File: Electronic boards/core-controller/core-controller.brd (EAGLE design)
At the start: 100 x 80 mm, 15 parts, among them IC1 ATMEGA88-THIN

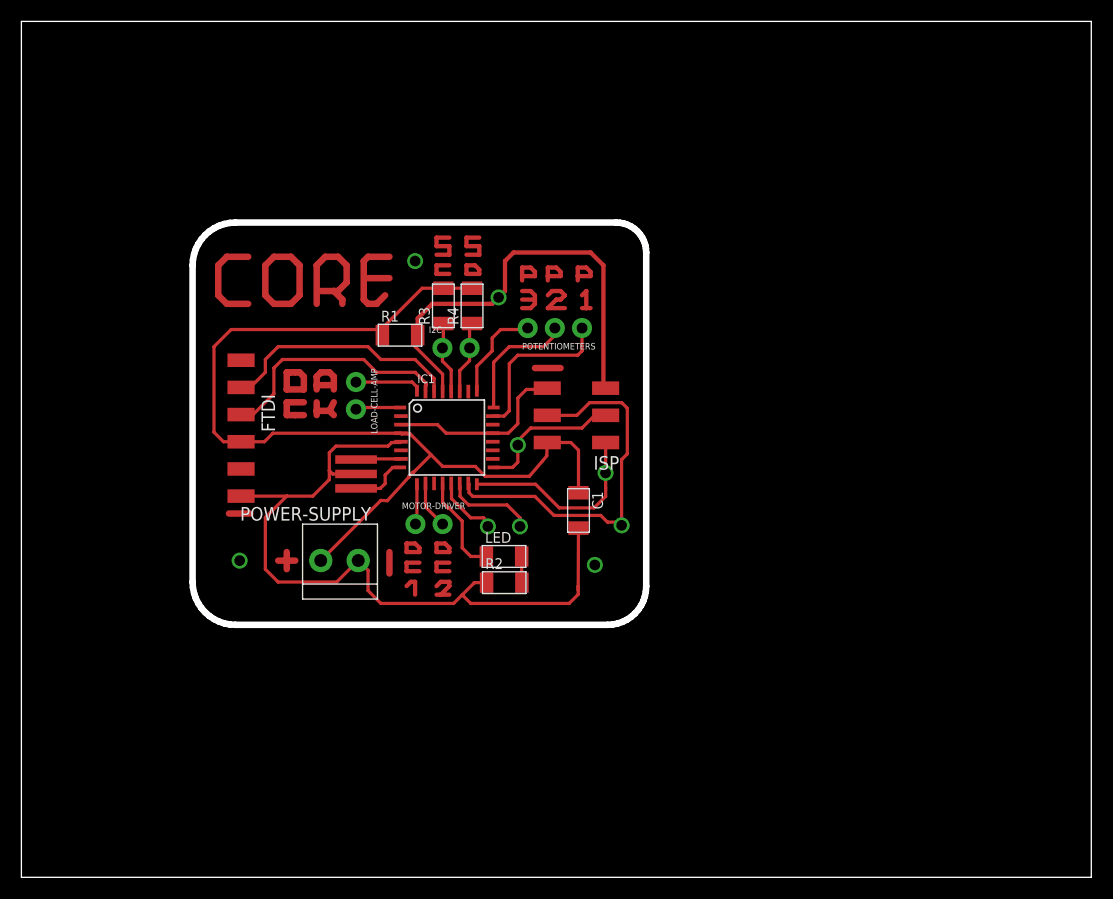
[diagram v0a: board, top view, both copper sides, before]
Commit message: Created folder for First Prototype and updated Core Controller board (with dc driver in itself, hence dc driver board is no more)
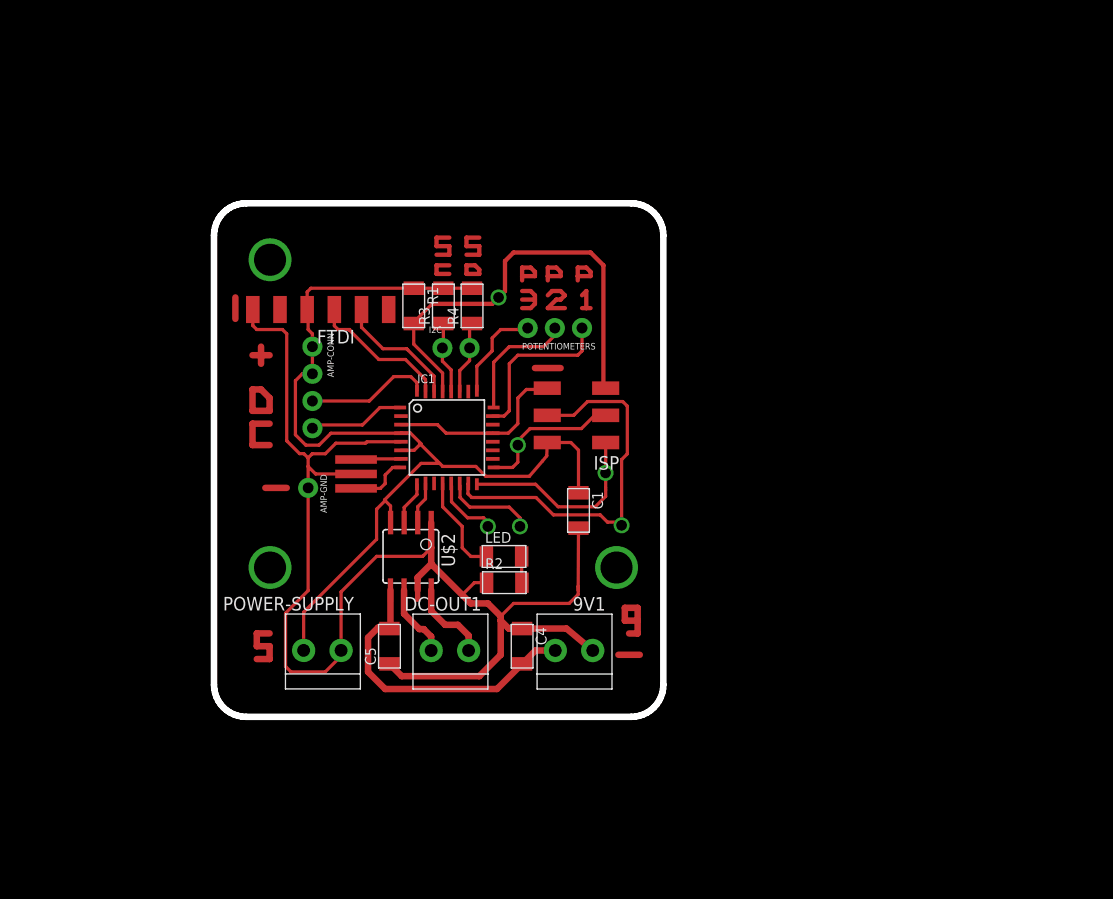
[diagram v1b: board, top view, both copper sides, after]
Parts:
- removed LOAD-CELL-AMP, MOTOR-DRIVER: (no value), SparkFun-Connectors:1X02_NO_SILK
- added 9V1, DC-OUT1: TERM-1X02-FABLAB, fab:ED555DS-2DS
- added AMP-CONN: (no value), SparkFun-Connectors:1X04_NO_SILK
- added AMP-GND: (no value), SparkFun-Connectors:1X01_NO_SILK
- added C4: 10uf, fab:C1206FAB
- added C5: 1uf, fab:C1206FAB
- added U$2: A4953, fab:SOIC8
- moved FTDI 13.4 mm to (28.0, 53.1), turned to 90 degrees
- moved POWER-SUPPLY 8.55 mm to (28.1, 21.2)
- moved R1 3.02 mm to (36.7, 53.4), turned to 270 degrees
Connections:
- removed net VCC: IC1.6
- new net OUT1: DC-OUT1.2, U$2.6
- new net OUT2: DC-OUT1.1, U$2.8
- new net VDD: 9V1.2, C4.2, C5.2, U$2.5
- net 5V: now also AMP-CONN.1, AMP-CONN.2, IC1.6, U$2.4
- net CLK: now also AMP-CONN.4; no longer LOAD-CELL-AMP.2
- net DAT: now also AMP-CONN.3; no longer LOAD-CELL-AMP.1
- net DC-IN-1: now also U$2.3; no longer MOTOR-DRIVER.1
- net DC-IN-2: now also U$2.2; no longer MOTOR-DRIVER.2
- net GND: now also 9V1.1, AMP-GND.1, C4.1, C5.1, U$2.1, U$2.7
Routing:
- net GND: track 90.6 -> 151.2 mm
- net VDD: track 0.00 -> 29.0 mm
- net N$30: track 13.3 -> 0.00 mm
- net N$31: track 12.9 -> 0.00 mm
- net RXD: track 22.8 -> 11.8 mm
- net TXD: track 22.6 -> 13.3 mm
- net N$29: track 9.06 -> 0.00 mm
- net N$32: track 8.66 -> 0.00 mm
- net OUT2: track 0.00 -> 7.80 mm
- net OUT1: track 0.00 -> 6.93 mm
- net N$54: track 0.00 -> 6.80 mm
- net DAT: track 6.24 -> 11.7 mm
- net CLK: track 4.20 -> 9.00 mm
- net N$4: track 1.60 -> 6.00 mm
- net N$11: track 4.40 -> 0.00 mm, vias 0 -> 1
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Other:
- board size 100 x 80 mm -> 42 x 48 mm
